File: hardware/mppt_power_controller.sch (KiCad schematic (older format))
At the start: 55 parts, among them J1 Solar Input, J2 USB_B_Micro, J3 Conn_ARM_JTAG_SWD_10, J4 Battery, J5 Curiosity Board, Q1 Q_NMOS_GSD, Q2 Q_NMOS_GSD, U1 INA233, U2 PX3519, U3 ATSAMD21G18A-AUT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

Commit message: Fix the footprints for a few components.
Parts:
- C4: footprint (none) -> Capacitor_SMD:C_0603_1608Metric_Pad1.05x0.95mm_HandSolder
- L1: footprint Inductor_SMD:L_Taiyo-Yuden_NR-10050_HandSoldering -> Inductor_SMD:L_Taiyo-Yuden_NR-10050_9.8x10.0mm_HandSoldering
- L2: footprint Inductors:Inductor_Taiyo-Yuden_NR-80xx_HandSoldering -> Inductor_SMD:L_Taiyo-Yuden_NR-80xx_HandSoldering
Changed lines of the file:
@@
 F 0 "L1" V 6105 3170 50  0000 C CNN
 F 1 "47uH" V 6014 3170 50  0000 C CNN
-F 2 "Inductor_SMD:L_Taiyo-Yuden_NR-10050_HandSoldering" H 5920 3170 50  0001 C CNN
+F 2 "Inductor_SMD:L_Taiyo-Yuden_NR-10050_9.8x10.0mm_HandSoldering" H 5920 3170 50  0001 C CNN
 F 3 "~" H 5920 3170 50  0001 C CNN
 F 4 "NR10050T470M" V 5920 3170 50  0001 C CNN "P/N"
@@
 F 0 "L2" V 10155 6510 50  0000 C CNN
 F 1 "10uH" V 10064 6510 50  0000 C CNN
-F 2 "Inductors:Inductor_Taiyo-Yuden_NR-80xx_HandSoldering" H 9970 6510 50  0001 C CNN
+F 2 "Inductor_SMD:L_Taiyo-Yuden_NR-80xx_HandSoldering" H 9970 6510 50  0001 C CNN
 F 3 "" H 9970 6510 50  0001 C CNN
 F 4 "NR8040T100M" V 9970 6510 60  0001 C CNN "part number"
@@
 F 0 "C4" V 4341 3850 50  0000 C CNN
 F 1 "1nF" V 4432 3850 50  0000 C CNN
-F 2 "" H 4570 3850 50  0001 C CNN
+F 2 "Capacitor_SMD:C_0603_1608Metric_Pad1.05x0.95mm_HandSolder" H 4570 3850 50  0001 C CNN
 F 3 "~" H 4570 3850 50  0001 C CNN
 	1    4570 3850

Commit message: Add four M3 mounting holes so I dont hate myself later.
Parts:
- added H1, H2, H3, H4: MountingHole, MountingHole:MountingHole_3.2mm_M3, symbol Mechanical:MountingHole
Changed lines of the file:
@@
 encoding utf-8
 Sheet 1 1
-Title ""
-Date ""
-Rev ""
+Title "PV Maximum Power Point Tracker"
+Date "2019-10-23"
+Rev "1"
 Comp ""
 Comment1 ""
@@
 Wire Wire Line
 	9240 3170 9280 3170
+$Comp
+L Mechanical:MountingHole H1
+U 1 1 5DB201BC
+P 12000 3600
+F 0 "H1" H 12100 3646 50  0000 L CNN
+F 1 "MountingHole" H 12100 3555 50  0000 L CNN
+F 2 "MountingHole:MountingHole_3.2mm_M3" H 12000 3600 50  0001 C CNN
+F 3 "~" H 12000 3600 50  0001 C CNN
+	1    12000 3600
+	1    0    0    -1
+$EndComp
+$Comp
+L Mechanical:MountingHole H2
+U 1 1 5DB20529
+P 12000 3800
+F 0 "H2" H 12100 3846 50  0000 L CNN
+F 1 "MountingHole" H 12100 3755 50  0000 L CNN
+F 2 "MountingHole:MountingHole_3.2mm_M3" H 12000 3800 50  0001 C CNN
+F 3 "~" H 12000 3800 50  0001 C CNN
+	1    12000 3800
+	1    0    0    -1
+$EndComp
+$Comp
+L Mechanical:MountingHole H3
+U 1 1 5DB208D6
+P 12000 4000
+F 0 "H3" H 12100 4046 50  0000 L CNN
+F 1 "MountingHole" H 12100 3955 50  0000 L CNN
+F 2 "MountingHole:MountingHole_3.2mm_M3" H 12000 4000 50  0001 C CNN
+F 3 "~" H 12000 4000 50  0001 C CNN
+	1    12000 4000
+	1    0    0    -1
+$EndComp
+$Comp
+L Mechanical:MountingHole H4
+U 1 1 5DB20BBD
+P 12000 4200
+F 0 "H4" H 12100 4246 50  0000 L CNN
+F 1 "MountingHole" H 12100 4155 50  0000 L CNN
+F 2 "MountingHole:MountingHole_3.2mm_M3" H 12000 4200 50  0001 C CNN
+F 3 "~" H 12000 4200 50  0001 C CNN
+	1    12000 4200
+	1    0    0    -1
+$EndComp
 $EndSCHEMATC

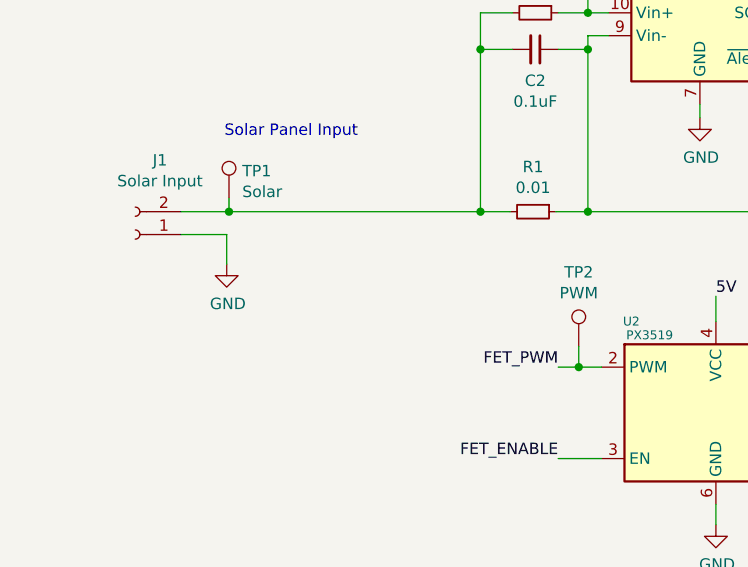
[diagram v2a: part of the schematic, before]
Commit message: Add some input capacitance for the solar panel
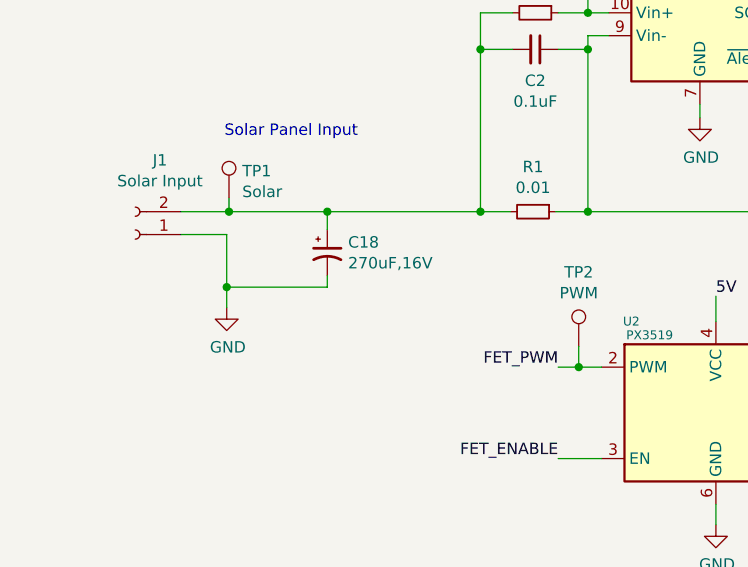
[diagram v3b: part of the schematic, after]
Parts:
- added C18: 270uF,16V, Capacitor_SMD:CP_Elec_8x6.9, symbol Device:CP1_Small
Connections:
- net GND: now also C18.2
- net at C2.2, J1.2 (Pin_2), R1.2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: now also C18.1
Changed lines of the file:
@@
 L power:GND #PWR02
 U 1 1 5DAA1D3F
-P 1550 3400
-F 0 "#PWR02" H 1550 3150 50  0001 C CNN
-F 1 "GND" H 1555 3227 50  0000 C CNN
-F 2 "" H 1550 3400 50  0001 C CNN
-F 3 "" H 1550 3400 50  0001 C CNN
-	1    1550 3400
+P 1550 3590
+F 0 "#PWR02" H 1550 3340 50  0001 C CNN
+F 1 "GND" H 1555 3417 50  0000 C CNN
+F 2 "" H 1550 3590 50  0001 C CNN
+F 3 "" H 1550 3590 50  0001 C CNN
+	1    1550 3590
 	1    0    0    -1
 $EndComp
@@
 	9110 3270 9110 3360
 Wire Wire Line
-	1550 3270 1550 3400
+	1550 3270 1550 3500
 Wire Wire Line
 	1350 3170 1560 3170
@@
 Connection ~ 1560 3170
 Wire Wire Line
-	1560 3170 2660 3170
+	1560 3170 1990 3170
 $Comp
 L Connector:TestPoint TP2
@@
 	1    0    0    -1
 $EndComp
+$Comp
+L Device:CP1_Small C18
+U 1 1 5DB2303E
+P 1990 3350
+F 0 "C18" H 2081 3396 50  0000 L CNN
+F 1 "270uF,16V" H 2081 3305 50  0000 L CNN
+F 2 "Capacitor_SMD:CP_Elec_8x6.9" H 1990 3350 50  0001 C CNN
+F 3 "~" H 1990 3350 50  0001 C CNN
+F 4 "16SVPF270M" H 1990 3350 50  0001 C CNN "P/N"
+	1    1990 3350
+	1    0    0    -1
+$EndComp
+Wire Wire Line
+	1990 3170 1990 3250
+Connection ~ 1990 3170
+Wire Wire Line
+	1990 3170 2660 3170
+Wire Wire Line
+	1990 3450 1990 3500
+Wire Wire Line
+	1990 3500 1550 3500
+Connection ~ 1550 3500
+Wire Wire Line
+	1550 3500 1550 3590
 $EndSCHEMATC

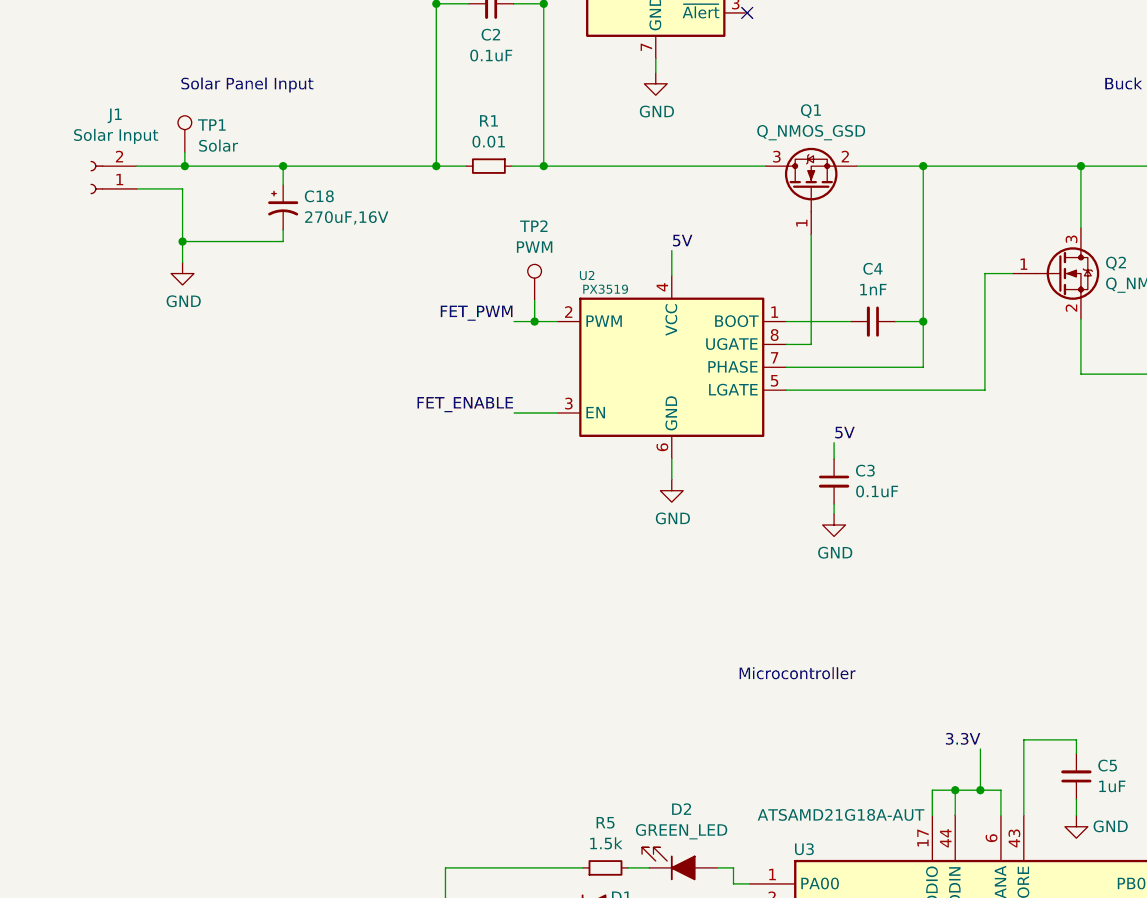
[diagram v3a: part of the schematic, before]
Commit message: Route a good amount of the microcontroller as well as the 5V power supply.
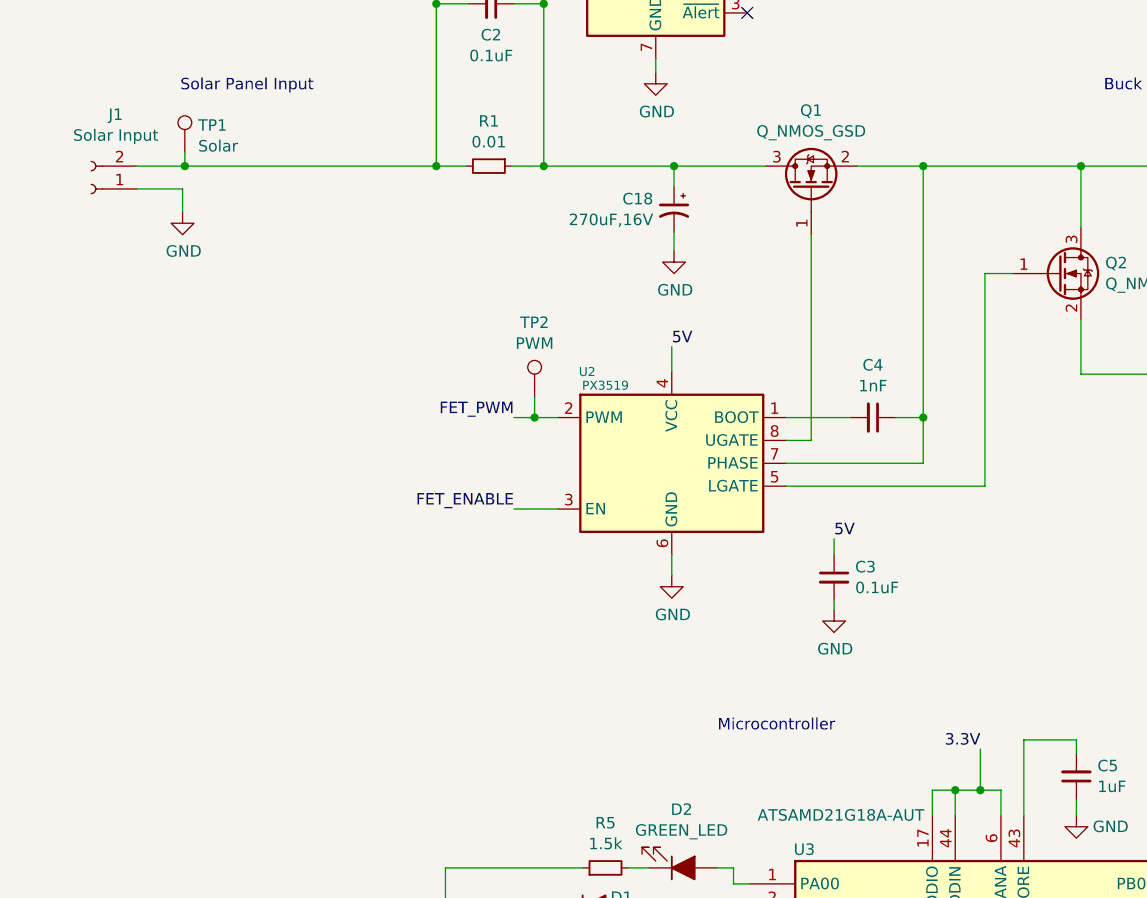
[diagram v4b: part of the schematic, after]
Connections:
- net at C2.2, J1.2 (Pin_2), R1.2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: no longer C18.1
- net at C2.1, Q1.3 (D), R1.1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: now also C18.1
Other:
- moved on the sheet: C18, C3, C4, TP2, U2
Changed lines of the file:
@@
 Text Notes 10150 5980 0    50   ~ 0
 5V@900mA from SMPS/battery
-Text Notes 3980 5430 0    50   ~ 0
+Text Notes 3890 5650 0    50   ~ 0
 Microcontroller
 $Comp
@@
 L power:GND #PWR02
 U 1 1 5DAA1D3F
-P 1550 3590
-F 0 "#PWR02" H 1550 3340 50  0001 C CNN
-F 1 "GND" H 1555 3417 50  0000 C CNN
-F 2 "" H 1550 3590 50  0001 C CNN
-F 3 "" H 1550 3590 50  0001 C CNN
-	1    1550 3590
+P 1550 3370
+F 0 "#PWR02" H 1550 3120 50  0001 C CNN
+F 1 "GND" H 1555 3197 50  0000 C CNN
+F 2 "" H 1550 3370 50  0001 C CNN
+F 3 "" H 1550 3370 50  0001 C CNN
+	1    1550 3370
 	1    0    0    -1
 $EndComp
@@
 	3620 2760 3620 2700
 Wire Wire Line
-	3130 3170 4100 3170
+	3130 3170 3700 3170
 Connection ~ 3130 3170
 Wire Wire Line
@@
 Wire Wire Line
 	9110 3270 9110 3360
-Wire Wire Line
-	1550 3270 1550 3500
 Wire Wire Line
 	1350 3170 1560 3170
@@
 	2700 6240 2700 6410
 Connection ~ 2700 6410
-$Comp
-L Driver_FET:PX3519 U2
-U 1 1 5DB16487
-P 3690 4050
-F 0 "U2" H 3320 4450 39  0000 C CNN
-F 1 "PX3519" H 3400 4390 39  0000 C CNN
-F 2 "Package_SON:WSON-8-1EP_3x3mm_P0.5mm_EP1.6x2.0mm" H 3790 4050 39  0001 C CNN
-F 3 "" H 3690 4050 39  0001 C CNN
-	1    3690 4050
-	1    0    0    -1
-$EndComp
-$Comp
-L Device:C_Small C4
-U 1 1 5DB1884D
-P 4570 3850
-F 0 "C4" V 4341 3850 50  0000 C CNN
-F 1 "1nF" V 4432 3850 50  0000 C CNN
-F 2 "Capacitor_SMD:C_0603_1608Metric_Pad1.05x0.95mm_HandSolder" H 4570 3850 50  0001 C CNN
-F 3 "~" H 4570 3850 50  0001 C CNN
-	1    4570 3850
-	0    1    1    0
-$EndComp
-Wire Wire Line
-	4190 3850 4470 3850
-Wire Wire Line
-	4790 4050 4790 3850
-Wire Wire Line
-	4790 3850 4790 3170
-Connection ~ 4790 3850
 Connection ~ 4790 3170
 Wire Wire Line
 	4790 3170 5480 3170
-Wire Wire Line
-	4190 4050 4790 4050
-Wire Wire Line
-	4670 3850 4790 3850
-Wire Wire Line
-	4190 3950 4300 3950
-Wire Wire Line
-	4300 3950 4300 3470
-Wire Wire Line
-	4190 4150 5060 4150
-Wire Wire Line
-	5060 4150 5060 3640
-Wire Wire Line
-	5060 3640 5180 3640
-Wire Wire Line
-	3190 3850 3090 3850
-Wire Wire Line
-	3190 4250 3000 4250
-$Comp
-L power:GND #PWR07
-U 1 1 5DB27865
-P 3690 4540
-F 0 "#PWR07" H 3690 4290 50  0001 C CNN
-F 1 "GND" H 3695 4367 50  0000 C CNN
-F 2 "" H 3690 4540 50  0001 C CNN
-F 3 "" H 3690 4540 50  0001 C CNN
-	1    3690 4540
-	1    0    0    -1
-$EndComp
-Wire Wire Line
-	3690 4540 3690 4450
-Wire Wire Line
-	3690 3650 3690 3540
-Text Label 3690 3540 0    50   ~ 0
-5V
-Text Label 4400 4380 0    50   ~ 0
-5V
-Wire Wire Line
-	4400 4650 4400 4690
-$Comp
-L power:GND #PWR09
-U 1 1 5DB2980E
-P 4400 4690
-F 0 "#PWR09" H 4400 4440 50  0001 C CNN
-F 1 "GND" H 4405 4517 50  0000 C CNN
-F 2 "" H 4400 4690 50  0001 C CNN
-F 3 "" H 4400 4690 50  0001 C CNN
-	1    4400 4690
-	1    0    0    -1
-$EndComp
-$Comp
-L Device:C_Small C3
-U 1 1 5DB2981C
-P 4400 4550
-F 0 "C3" H 4492 4596 50  0000 L CNN
-F 1 "0.1uF" H 4492 4505 50  0000 L CNN
-F 2 "Capacitor_SMD:C_0603_1608Metric_Pad1.05x0.95mm_HandSolder" H 4400 4550 50  0001 C CNN
-F 3 "~" H 4400 4550 50  0001 C CNN
-	1    4400 4550
-	1    0    0    -1
-$EndComp
-Wire Wire Line
-	4400 4450 4400 4380
-Text Label 3000 3850 2    50   ~ 0
-FET_PWM
-Text Label 3000 4250 2    50   ~ 0
-FET_ENABLE
 Wire Wire Line
 	4030 7310 3900 7310
@@
 	1560 3110 1560 3170
 Connection ~ 1560 3170
-Wire Wire Line
-	1560 3170 1990 3170
-$Comp
-L Connector:TestPoint TP2
-U 1 1 5DB2FB40
-P 3090 3760
-F 0 "TP2" H 3090 4085 50  0000 C CNN
-F 1 "PWM" H 3090 3994 50  0000 C CNN
-F 2 "TestPoint:TestPoint_Keystone_5019_Minature" H 3290 3760 50  0001 C CNN
-F 3 "~" H 3290 3760 50  0001 C CNN
-F 4 "Keystone 5019" H 3090 3760 50  0001 C CNN "P/N"
-	1    3090 3760
-	1    0    0    -1
-$EndComp
-Wire Wire Line
-	3090 3760 3090 3850
-Connection ~ 3090 3850
-Wire Wire Line
-	3090 3850 3000 3850
 $Comp
 L Connector:Conn_01x05_Male J5
@@
 L Device:CP1_Small C18
 U 1 1 5DB2303E
-P 1990 3350
-F 0 "C18" H 2081 3396 50  0000 L CNN
-F 1 "270uF,16V" H 2081 3305 50  0000 L CNN
-F 2 "Capacitor_SMD:CP_Elec_8x6.9" H 1990 3350 50  0001 C CNN
-F 3 "~" H 1990 3350 50  0001 C CNN
-F 4 "16SVPF270M" H 1990 3350 50  0001 C CNN "P/N"
-	1    1990 3350
-	1    0    0    -1
-$EndComp
-Wire Wire Line
-	1990 3170 1990 3250
-Connection ~ 1990 3170
-Wire Wire Line
-	1990 3170 2660 3170
-Wire Wire Line
-	1990 3450 1990 3500
-Wire Wire Line
-	1990 3500 1550 3500
-Connection ~ 1550 3500
-Wire Wire Line
-	1550 3500 1550 3590
+P 3700 3360
+F 0 "C18" H 3791 3406 50  0000 L CNN
+F 1 "270uF,16V" H 3791 3315 50  0000 L CNN
+F 2 "Capacitor_SMD:CP_Elec_8x6.9" H 3700 3360 50  0001 C CNN
+F 3 "~" H 3700 3360 50  0001 C CNN
+F 4 "16SVPF270M" H 3700 3360 50  0001 C CNN "P/N"
+	1    3700 3360
+	-1   0    0    -1
+$EndComp
+$Comp
+L power:GND #PWR09
+U 1 1 5DB2980E
+P 4400 5110
+F 0 "#PWR09" H 4400 4860 50  0001 C CNN
+F 1 "GND" H 4405 4937 50  0000 C CNN
+F 2 "" H 4400 5110 50  0001 C CNN
+F 3 "" H 4400 5110 50  0001 C CNN
+	1    4400 5110
+	1    0    0    -1
+$EndComp
+Wire Wire Line
+	3090 4270 3000 4270
+Connection ~ 3090 4270
+Wire Wire Line
+	3090 4180 3090 4270
+$Comp
+L Connector:TestPoint TP2
+U 1 1 5DB2FB40
+P 3090 4180
+F 0 "TP2" H 3090 4505 50  0000 C CNN
+F 1 "PWM" H 3090 4414 50  0000 C CNN
+F 2 "TestPoint:TestPoint_Keystone_5019_Minature" H 3290 4180 50  0001 C CNN
+F 3 "~" H 3290 4180 50  0001 C CNN
+F 4 "Keystone 5019" H 3090 4180 50  0001 C CNN "P/N"
+	1    3090 4180
+	1    0    0    -1
+$EndComp
+Text Label 3000 4670 2    50   ~ 0
+FET_ENABLE
+Text Label 3000 4270 2    50   ~ 0
+FET_PWM
+Wire Wire Line
+	4400 4870 4400 4800
+$Comp
+L Device:C_Small C3
+U 1 1 5DB2981C
+P 4400 4970
+F 0 "C3" H 4492 5016 50  0000 L CNN
+F 1 "0.1uF" H 4492 4925 50  0000 L CNN
+F 2 "Capacitor_SMD:C_0603_1608Metric_Pad1.05x0.95mm_HandSolder" H 4400 4970 50  0001 C CNN
+F 3 "~" H 4400 4970 50  0001 C CNN
+	1    4400 4970
+	1    0    0    -1
+$EndComp
+Wire Wire Line
+	4400 5070 4400 5110
+Text Label 4400 4800 0    50   ~ 0
+5V
+Text Label 3690 3960 0    50   ~ 0
+5V
+Wire Wire Line
+	3690 4070 3690 3960
+Wire Wire Line
+	3690 4960 3690 4870
+$Comp
+L power:GND #PWR07
+U 1 1 5DB27865
+P 3690 4960
+F 0 "#PWR07" H 3690 4710 50  0001 C CNN
+F 1 "GND" H 3695 4787 50  0000 C CNN
+F 2 "" H 3690 4960 50  0001 C CNN
+F 3 "" H 3690 4960 50  0001 C CNN
+	1    3690 4960
+	1    0    0    -1
+$EndComp
+Wire Wire Line
+	3190 4670 3000 4670
+Wire Wire Line
+	3190 4270 3090 4270
+Wire Wire Line
+	4190 4570 5060 4570
+Wire Wire Line
+	4190 4370 4300 4370
+Wire Wire Line
+	4670 4270 4790 4270
+Wire Wire Line
+	4190 4470 4790 4470
+Wire Wire Line
+	4790 4270 4790 3170
+Wire Wire Line
+	4790 4470 4790 4270
+Wire Wire Line
+	4190 4270 4470 4270
+Connection ~ 4790 4270
+$Comp
+L Device:C_Small C4
+U 1 1 5DB1884D
+P 4570 4270
+F 0 "C4" V 4341 4270 50  0000 C CNN
+F 1 "1nF" V 4432 4270 50  0000 C CNN
+F 2 "Capacitor_SMD:C_0603_1608Metric_Pad1.05x0.95mm_HandSolder" H 4570 4270 50  0001 C CNN
+F 3 "~" H 4570 4270 50  0001 C CNN
+	1    4570 4270
+	0    1    1    0
+$EndComp
+$Comp
+L Driver_FET:PX3519 U2
+U 1 1 5DB16487
+P 3690 4470
+F 0 "U2" H 3320 4870 39  0000 C CNN
+F 1 "PX3519" H 3400 4810 39  0000 C CNN
+F 2 "Package_SON:WSON-8-1EP_3x3mm_P0.5mm_EP1.6x2.0mm" H 3790 4470 39  0001 C CNN
+F 3 "" H 3690 4470 39  0001 C CNN
+	1    3690 4470
+	1    0    0    -1
+$EndComp
+Wire Wire Line
+	4300 3470 4300 4370
+Wire Wire Line
+	5060 3640 5180 3640
+Wire Wire Line
+	5060 3640 5060 4570
+Wire Wire Line
+	1560 3170 2660 3170
+Wire Wire Line
+	1550 3270 1550 3370
+$Comp
+L power:GND #PWR?
+U 1 1 5DB30CA4
+P 3700 3540
+F 0 "#PWR?" H 3700 3290 50  0001 C CNN
+F 1 "GND" H 3705 3367 50  0000 C CNN
+F 2 "" H 3700 3540 50  0001 C CNN
+F 3 "" H 3700 3540 50  0001 C CNN
+	1    3700 3540
+	1    0    0    -1
+$EndComp
+Wire Wire Line
+	3700 3460 3700 3540
+Wire Wire Line
+	3700 3260 3700 3170
+Connection ~ 3700 3170
+Wire Wire Line
+	3700 3170 4100 3170
 $EndSCHEMATC

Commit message: Change INA233 from "rescue" library to real library. Small mistake!
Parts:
- U1, U4: symbol mppt_power_controller-rescue:INA233-Analog_ADC -> Analog_ADC:INA233
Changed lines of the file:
@@
 $EndComp
 $Comp
-L mppt_power_controller-rescue:INA233-Analog_ADC U1
+L Analog_ADC:INA233 U1
 U 1 1 5DAF74FD
 P 3620 2200
@@
 	9060 1700 9060 1640
 $Comp
-L mppt_power_controller-rescue:INA233-Analog_ADC U4
+L Analog_ADC:INA233 U4
 U 1 1 5DB0D624
 P 9060 2200

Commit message: Move around 5V SMPS
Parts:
- U2: symbol Driver_FET:PX3519 -> mppt_power_controller-rescue:PX3519-Driver_FET
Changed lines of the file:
@@
 $EndComp
 $Comp
-L Driver_FET:PX3519 U2
+L mppt_power_controller-rescue:PX3519-Driver_FET U2
 U 1 1 5DB16487
 P 3690 4470
